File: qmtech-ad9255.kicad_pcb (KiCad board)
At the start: 4 copper layers, 70 x 85 mm, 78 parts

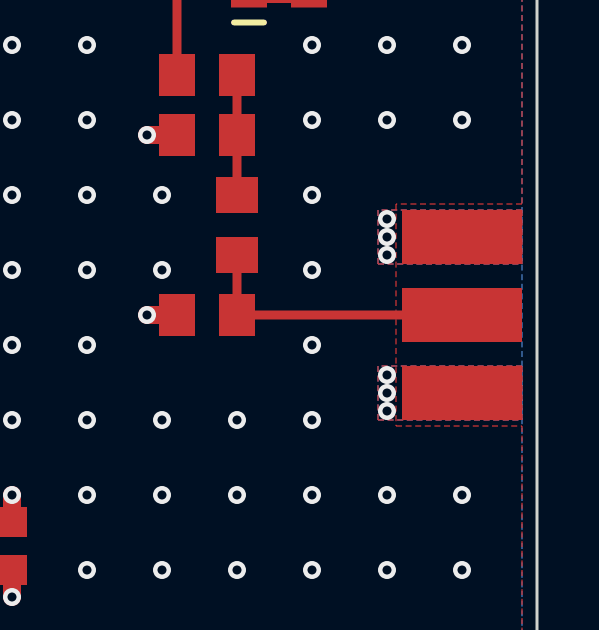
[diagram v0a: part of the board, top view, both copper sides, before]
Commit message: improve GND connection of SMA connector in qmtech-ad9255
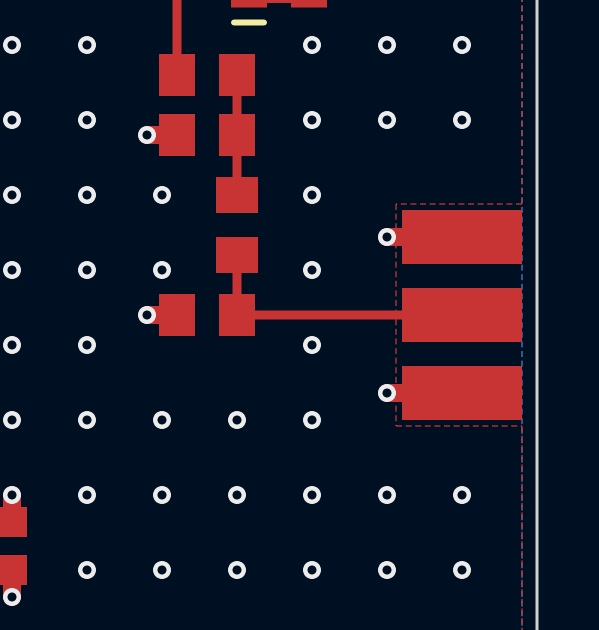
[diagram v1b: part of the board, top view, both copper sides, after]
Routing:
- net GND: track 87.8 -> 97.8 mm, vias 549 -> 545
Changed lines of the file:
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@@
   (segment (start 145.95 115.8) (end 145.95 113.75) (width 0.6) (layer "F.Cu") (net 3))
   (segment (start 170.95 115.8) (end 170.95 117) (width 0.6) (layer "F.Cu") (net 3))
+  (segment (start 190 114.1) (end 192.5 114.1) (width 0.6) (layer "F.Cu") (net 3))
   (segment (start 186 76.5) (end 185 76.5) (width 0.6) (layer "F.Cu") (net 3))
   (segment (start 165 95.5) (end 165.9 95.5) (width 0.6) (layer "F.Cu") (net 3))
@@
   (segment (start 145.95 115.8) (end 145.95 117) (width 0.6) (layer "F.Cu") (net 3))
   (segment (start 146 121.4) (end 146 120.3) (width 0.6) (layer "F.Cu") (net 3))
+  (segment (start 190 108.9) (end 192.5 108.9) (width 0.6) (layer "F.Cu") (net 3))
   (via (at 182.5 87.5) (size 0.6) (drill 0.3) (layers "F.Cu" "B.Cu") (remove_unused_layers) (keep_end_layers) (free) (zone_layer_connections "In1.Cu") (net 3))
   (via (at 165 112.5) (size 0.6) (drill 0.3) (layers "F.Cu" "B.Cu") (remove_unused_layers) (keep_end_layers) (free) (zone_layer_connections "In1.Cu") (net 3))
@@
   (via (at 192.5 105) (size 0.6) (drill 0.3) (layers "F.Cu" "B.Cu") (remove_unused_layers) (keep_end_layers) (free) (zone_layer_connections "In1.Cu") (net 3))
   (via (at 187.5 97.5) (size 0.6) (drill 0.3) (layers "F.Cu" "B.Cu") (remove_unused_layers) (keep_end_layers) (free) (zone_layer_connections "In1.Cu") (net 3))
-  (via (at 190 109.5) (size 0.6) (drill 0.3) (layers "F.Cu" "B.Cu") (remove_unused_layers) (keep_end_layers) (free) (zone_layer_connections "In1.Cu") (net 3))
   (via (at 192.5 95) (size 0.6) (drill 0.3) (layers "F.Cu" "B.Cu") (remove_unused_layers) (keep_end_layers) (free) (zone_layer_connections "In1.Cu") (net 3))
   (via (at 147.5 127.5) (size 0.6) (drill 0.3) (layers "F.Cu" "B.Cu") (remove_unused_layers) (keep_end_layers) (free) (zone_layer_connections "In1.Cu") (net 3))
@@
   (via (at 177.5 47.5) (size 0.6) (drill 0.3) (layers "F.Cu" "B.Cu") (remove_unused_layers) (keep_end_layers) (free) (zone_layer_connections "In1.Cu" "In2.Cu") (net 3))
   (via (at 151.8 106.5) (size 0.6) (drill 0.3) (layers "F.Cu" "B.Cu") (remove_unused_layers) (keep_end_layers) (free) (zone_layer_connections "In1.Cu") (net 3))
-  (via (at 190 113.5) (size 0.6) (drill 0.3) (layers "F.Cu" "B.Cu") (remove_unused_layers) (keep_end_layers) (free) (zone_layer_connections "In1.Cu") (net 3))
   (via (at 192.5 82.5) (size 0.6) (drill 0.3) (layers "F.Cu" "B.Cu") (remove_unused_layers) (keep_end_layers) (free) (zone_layer_connections "In1.Cu") (net 3))
   (via (at 132.5 112) (size 0.6) (drill 0.3) (layers "F.Cu" "B.Cu") (remove_unused_layers) (keep_end_layers) (free) (zone_layer_connections "In1.Cu") (net 3))
@@
   (via (at 148.7 58.3) (size 0.6) (drill 0.3) (layers "F.Cu" "B.Cu") (remove_unused_layers) (keep_end_layers) (free) (zone_layer_connections "In1.Cu") (net 3))
   (via (at 160 96.5) (size 0.6) (drill 0.3) (layers "F.Cu" "B.Cu") (remove_unused_layers) (keep_end_layers) (free) (zone_layer_connections "In1.Cu") (net 3))
-  (via (at 190 108.3) (size 0.6) (drill 0.3) (layers "F.Cu" "B.Cu") (remove_unused_layers) (keep_end_layers) (free) (zone_layer_connections "In1.Cu") (net 3))
   (via (at 157.5 100.5) (size 0.6) (drill 0.3) (layers "F.Cu" "B.Cu") (remove_unused_layers) (keep_end_layers) (free) (zone_layer_connections "In1.Cu") (net 3))
   (via (at 192.5 72.5) (size 0.6) (drill 0.3) (layers "F.Cu" "B.Cu") (remove_unused_layers) (keep_end_layers) (free) (zone_layer_connections "In1.Cu" "In2.Cu") (net 3))
@@
   (via (at 143.1 122.5) (size 0.6) (drill 0.3) (layers "F.Cu" "B.Cu") (remove_unused_layers) (keep_end_layers) (free) (zone_layer_connections "In1.Cu") (net 3))
   (via (at 180 75) (size 0.6) (drill 0.3) (layers "F.Cu" "B.Cu") (remove_unused_layers) (keep_end_layers) (free) (zone_layer_connections "In1.Cu" "In2.Cu") (net 3))
-  (via (at 190 114.7) (size 0.6) (drill 0.3) (layers "F.Cu" "B.Cu") (remove_unused_layers) (keep_end_layers) (free) (zone_layer_connections "In1.Cu") (net 3))
   (via (at 186 88) (size 0.6) (drill 0.3) (layers "F.Cu" "B.Cu") (remove_unused_layers) (keep_end_layers) (free) (zone_layer_connections "In1.Cu") (net 3))
   (via (at 167.5 52.5) (size 0.6) (drill 0.3) (layers "F.Cu" "B.Cu") (remove_unused_layers) (keep_end_layers) (free) (zone_layer_connections "In1.Cu" "In2.Cu") (net 3))
@@
   (via (at 177.5 67.5) (size 0.6) (drill 0.3) (layers "F.Cu" "B.Cu") (remove_unused_layers) (keep_end_layers) (free) (zone_layer_connections "In1.Cu" "In2.Cu") (net 3))
   (via (at 192.5 117.5) (size 0.6) (drill 0.3) (layers "F.Cu" "B.Cu") (remove_unused_layers) (keep_end_layers) (free) (zone_layer_connections "In1.Cu") (net 3))
+  (segment (start 190 108.9) (end 192.5 108.9) (width 0.6) (layer "B.Cu") (net 3))
+  (segment (start 190 114.1) (end 192.5 114.1) (width 0.6) (layer "B.Cu") (net 3))
   (segment (start 151.95 96.25) (end 152.6 95.6) (width 0.28) (layer "F.Cu") (net 4))
   (segment (start 152.6 95.6) (end 152.6 95) (width 0.28) (layer "F.Cu") (net 4))
@@
       )
     )
-  )
-  (zone (net 3) (net_name "GND") (layers "F&B.Cu") (hatch edge 0.5)
-    (priority 14)
-    (connect_pads yes (clearance 0.2))
-    (min_thickness 0.2) (filled_areas_thickness no)
-    (fill (thermal_gap 0.3) (thermal_bridge_width 0.6))
-    (polygon
-      (pts
-        (xy 194.5 109.8)
-        (xy 194.5 108)
-        (xy 189.7 108)
-        (xy 189.7 109.8)
-      )
-    )
-  )
-  (zone (net 3) (net_name "GND") (layers "F&B.Cu") (hatch edge 0.5)
-    (priority 14)
-    (connect_pads yes (clearance 0.2))
-    (min_thickness 0.2) (filled_areas_thickness no)
-    (fill (thermal_gap 0.3) (thermal_bridge_width 0.6))
-    (polygon
-      (pts
-        (xy 194.5 115)
-        (xy 194.5 113.2)
-        (xy 189.7 113.2)
-        (xy 189.7 115)
-      )
-    )

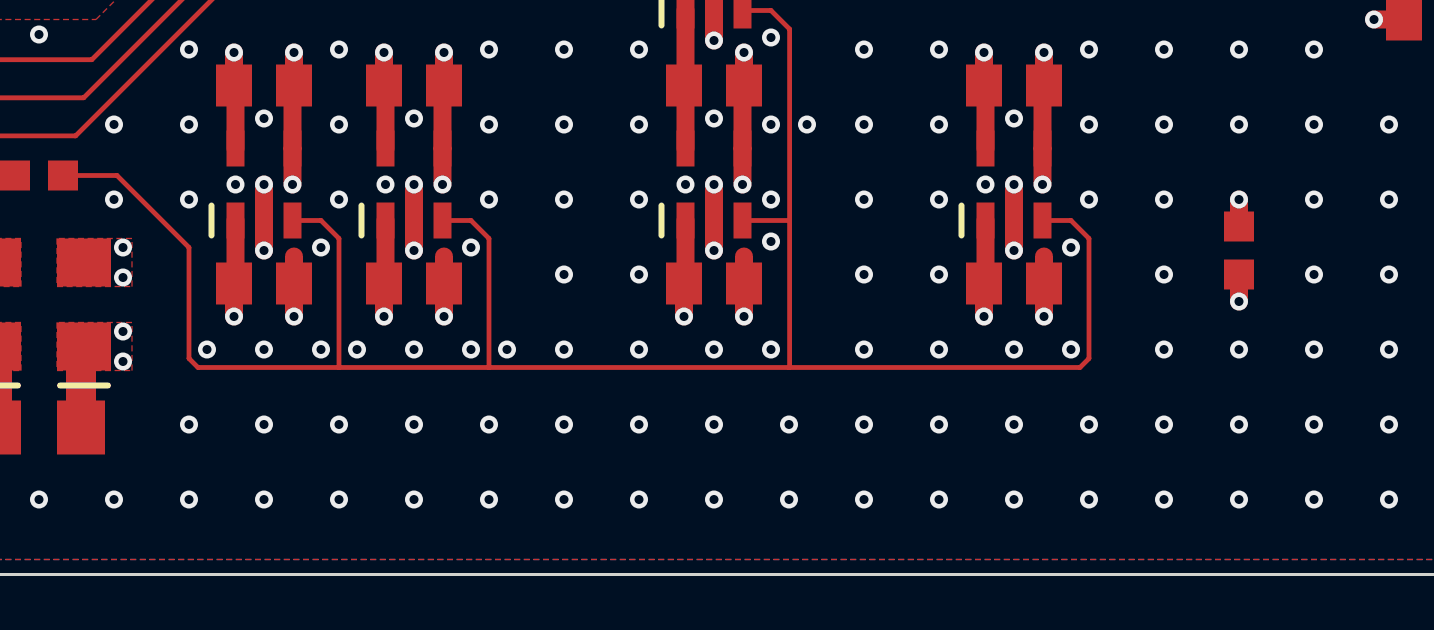
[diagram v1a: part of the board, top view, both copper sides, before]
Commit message: improve power planes in qmtech-ad9255
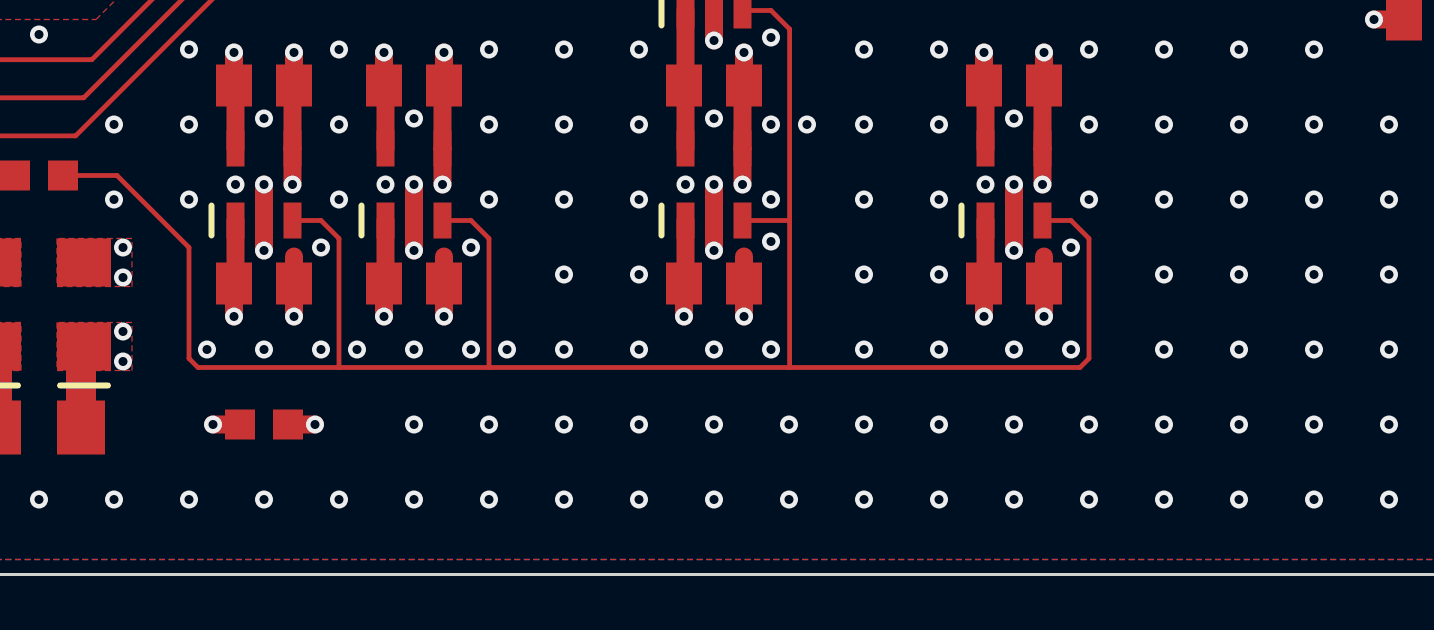
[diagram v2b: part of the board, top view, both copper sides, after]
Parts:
- moved R13 33.0 mm to (145.0, 125.0), turned to 0 degrees
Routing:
- net GND: vias 545 -> 544

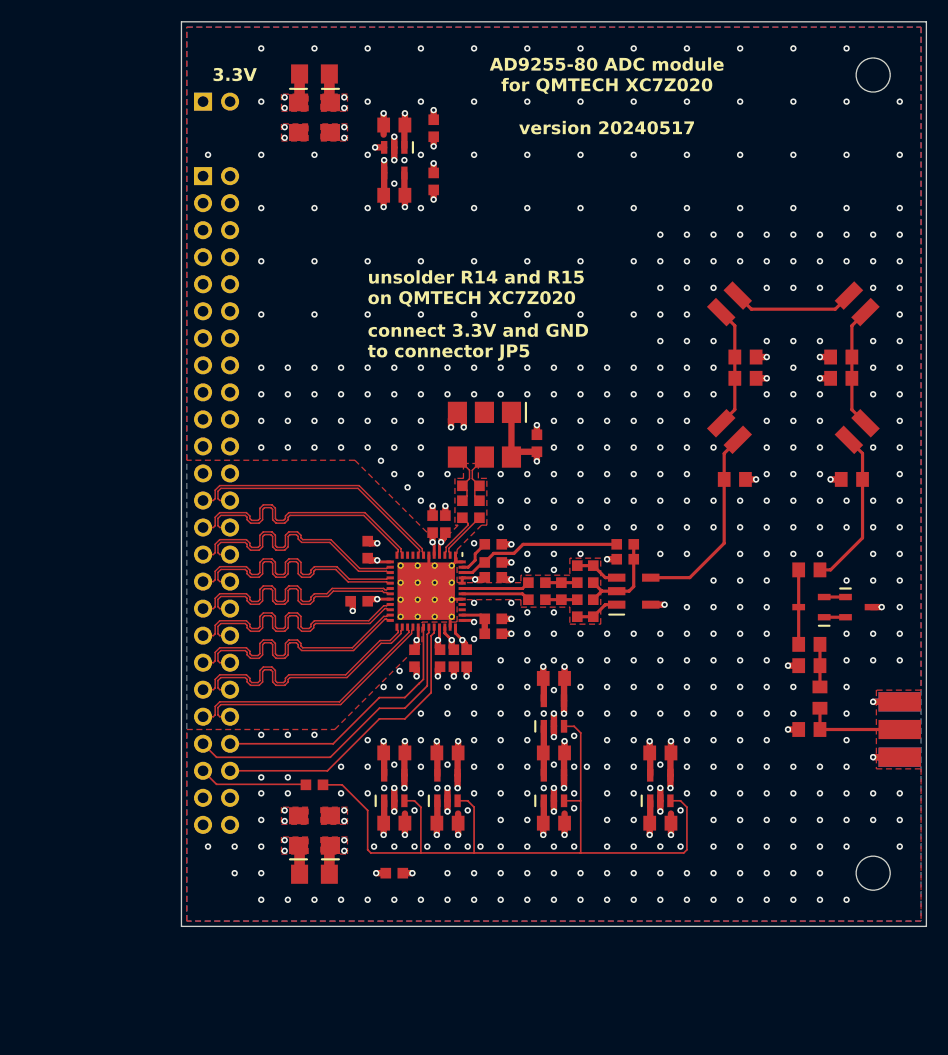
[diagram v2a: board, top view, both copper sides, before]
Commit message: improve 30 MHz LPF in qmtech-ad9255
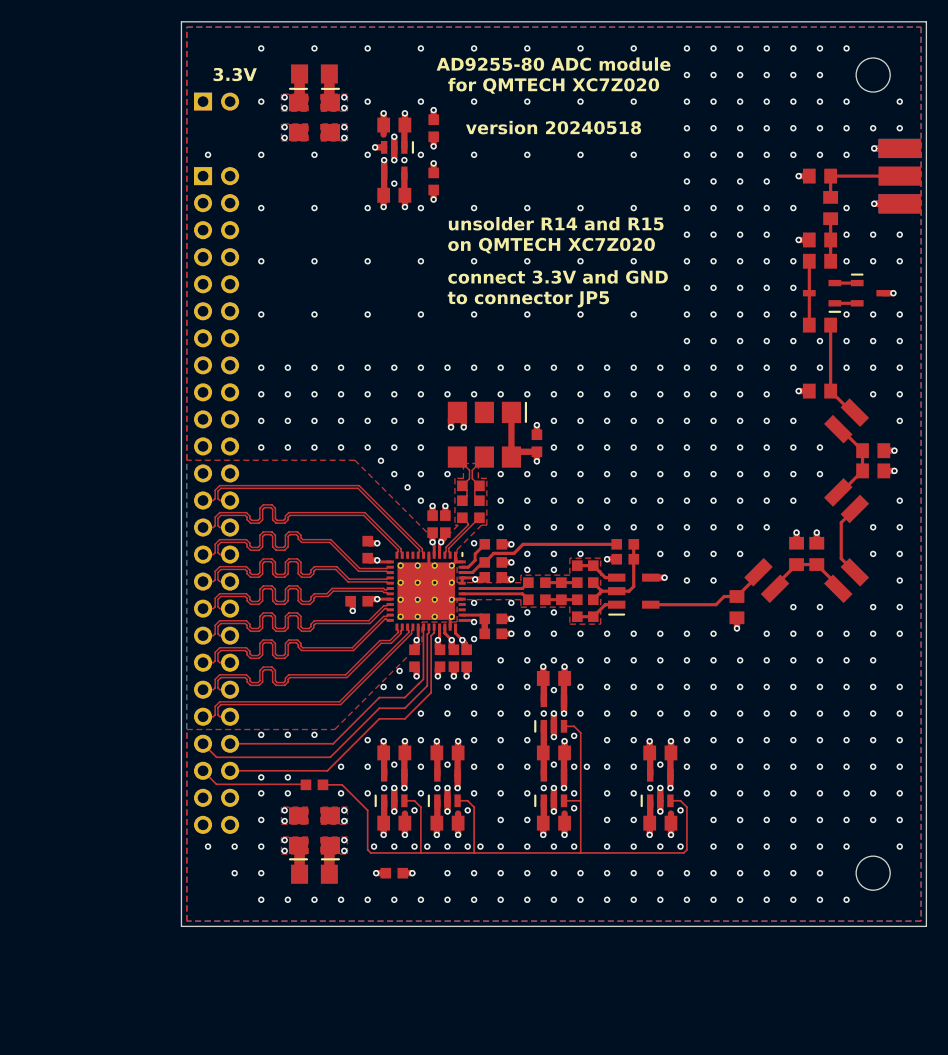
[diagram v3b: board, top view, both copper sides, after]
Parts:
- removed M1: , footprints:M3
- added H1: , footprints:M3, F.Cu at (190.0, 125.0)
- moved R15 52.0 mm to (185.0, 59.5)
- moved CN1 52.0 mm to (192.5, 59.5)
- moved R14 46.0 mm to (186.0, 62.5), turned to -90 degrees
- moved R16 40.0 mm to (185.0, 65.5)
- moved C33 36.0 mm to (185.0, 67.5)
- moved D2 29.5 mm to (189.7, 70.5)
- moved D1 29.5 mm to (185.2, 70.5)
- moved L3 28.2 mm to (187.5, 97.5)
- moved C34 23.0 mm to (185.0, 73.5)
- moved C38 19.7 mm to (184.7, 95.0), turned to 90 degrees
- moved L2 18.5 mm to (187.5, 90.0), turned to -45 degrees
- moved C39 17.2 mm to (182.8, 95.0), turned to 90 degrees
- moved L4 14.4 mm to (180.0, 97.5), turned to 135 degrees
- moved C40 12.0 mm to (177.2, 100.0), turned to -90 degrees
- moved C37 11.1 mm to (190.0, 87.2), turned to 0 degrees
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- renumbered M2 to H2
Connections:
- T1 pad 4: FLT5 -> GND
- T1 pad 6: GND -> FLT5
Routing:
- net FLT5: track 18.5 -> 11.5 mm
- net FLT1: track 15.0 -> 9.32 mm
- net FLT3: track 11.5 -> 7.00 mm
- net FLT4: track 11.5 -> 8.13 mm
- net FLT2: track 11.5 -> 8.13 mm
- net TVS1: track 7.00 -> 6.00 mm
- net ATT1: track 9.50 -> 8.50 mm
- net GND: track 97.8 -> 97.4 mm, vias 544 -> 576
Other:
- board text added: "version 20240518"
- board text removed: "version 20240517"

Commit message: improve mounting hole positions in qmtech-ad9255
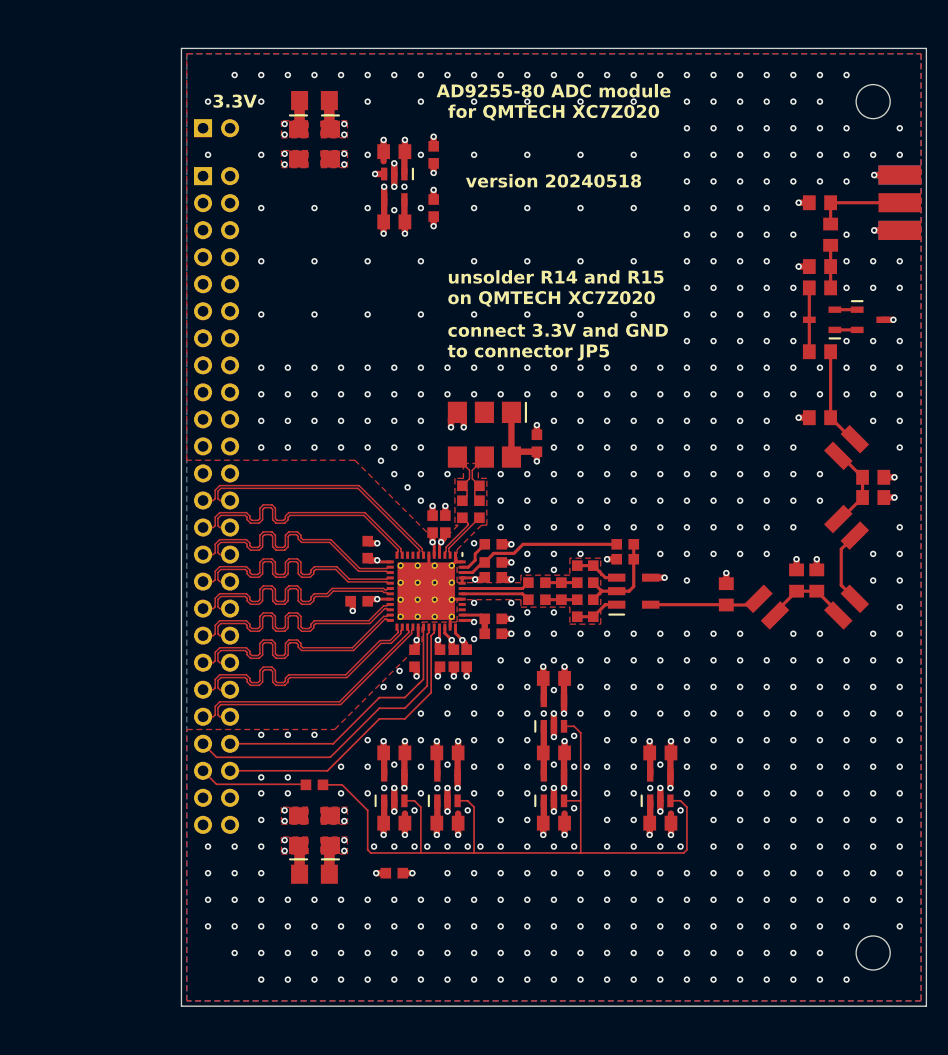
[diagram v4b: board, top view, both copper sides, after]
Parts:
- moved H1 7.50 mm to (190.0, 132.5)
- moved C27 2.50 mm to (145.0, 57.2)
- moved C28 2.50 mm to (145.0, 63.8)
- moved C31 2.50 mm to (136.0, 56.5)
- moved C32 2.50 mm to (139.0, 56.5)
- moved C33 2.50 mm to (185.0, 70.0)
- moved C34 2.50 mm to (185.0, 76.0)
- moved C35 2.50 mm to (185.0, 82.2)
- moved C36 2.50 mm to (190.0, 87.8)
- moved C37 2.50 mm to (190.0, 89.7)
- moved C38 2.50 mm to (184.7, 97.5)
- moved C39 2.50 mm to (182.8, 97.5)
- moved CN1 2.50 mm to (192.5, 62.0)
- moved CN3 2.50 mm to (128.3, 55.0)
- moved D1 2.50 mm to (185.2, 73.0)
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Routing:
- net FLT5: track 11.5 -> 10.4 mm
- net GND: vias 576 -> 658
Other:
- board size 70 x 85 mm -> 70 x 90 mm
